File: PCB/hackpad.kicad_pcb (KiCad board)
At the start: 2 copper layers, 50.3 x 60 mm, 9 parts, among them SW1 SW_Push, SW2 SW_Push, SW3 SW_Push, SW4 SW_Push, U1 XIAO-RP2040-DIP

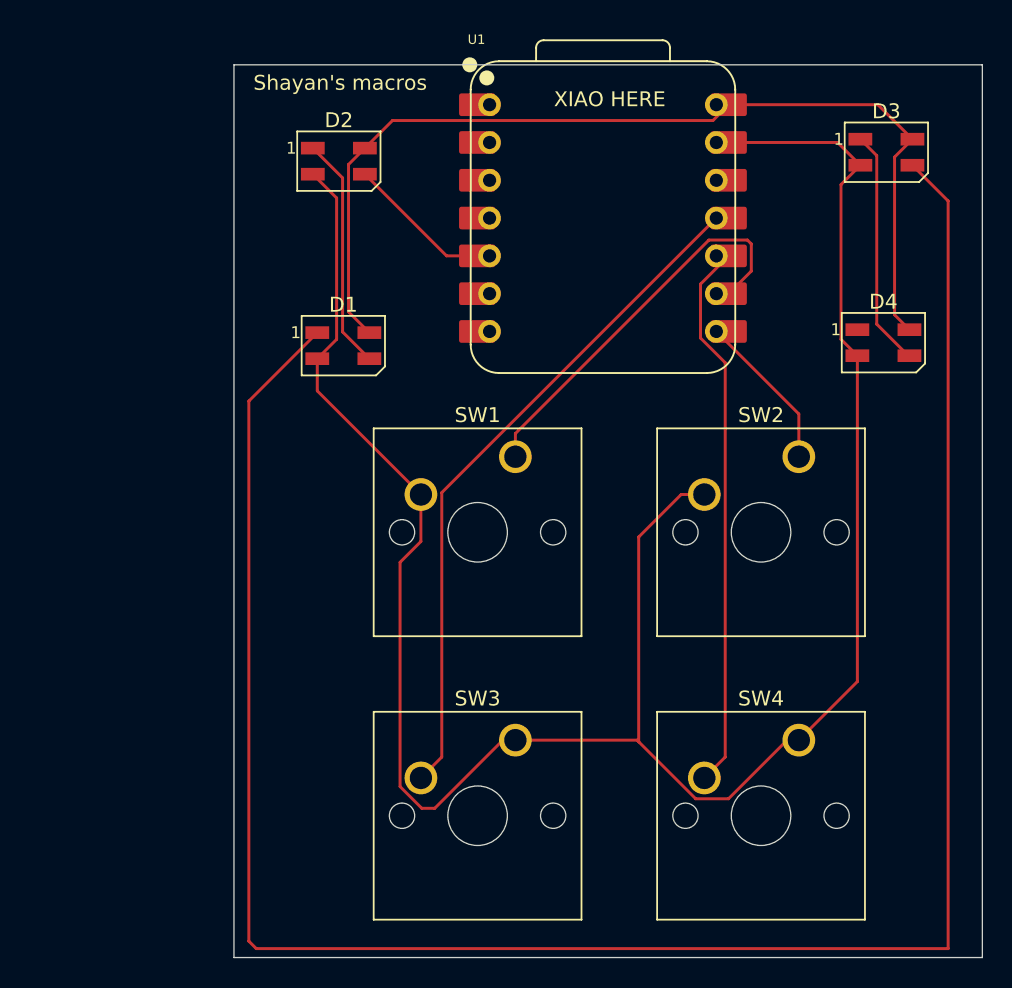
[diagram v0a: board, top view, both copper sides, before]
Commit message: Added rotary-encoder
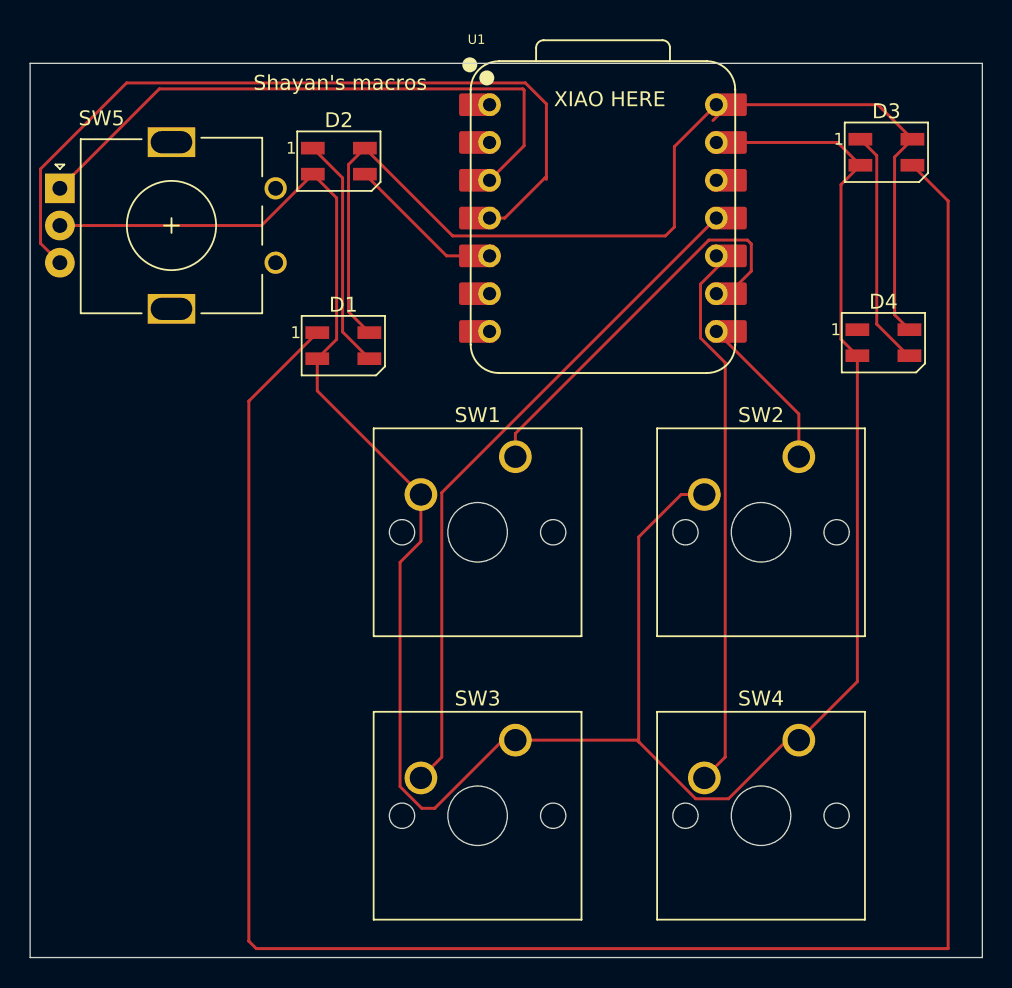
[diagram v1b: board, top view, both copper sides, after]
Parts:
- added SW5: RotaryEncoder, Rotary_Encoder:RotaryEncoder_Alps_EC11E_Vertical_H20mm, F.Cu at (76.7, 50.7)
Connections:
- U1 pad 3: unconnected-(U1-GPIO28/ADC2/A2-Pad3) -> Net-(U1-GPIO28/ADC2/A2)
- U1 pad 4: unconnected-(U1-GPIO29/ADC3/A3-Pad4) -> Net-(U1-GPIO29/ADC3/A3)
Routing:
- net Net-(U1-GPIO29/ADC3/A3): track 0.00 -> 54.7 mm
- net Net-(U1-GPIO28/ADC2/A2): track 0.00 -> 41.0 mm
- net GND: track 148.5 -> 166.9 mm
- net +5V: track 66.1 -> 74.8 mm
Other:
- board size 50.3 x 60 mm -> 64 x 60.1 mm
